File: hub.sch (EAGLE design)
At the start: 50 parts, among them IC1 SN65220DBV, IC2 SN65220DBV, IC3 SN65220DBV, IC4 SN65220DBV, IC5 SN65220DBV, U1 LM3526-L, X1 12MHz

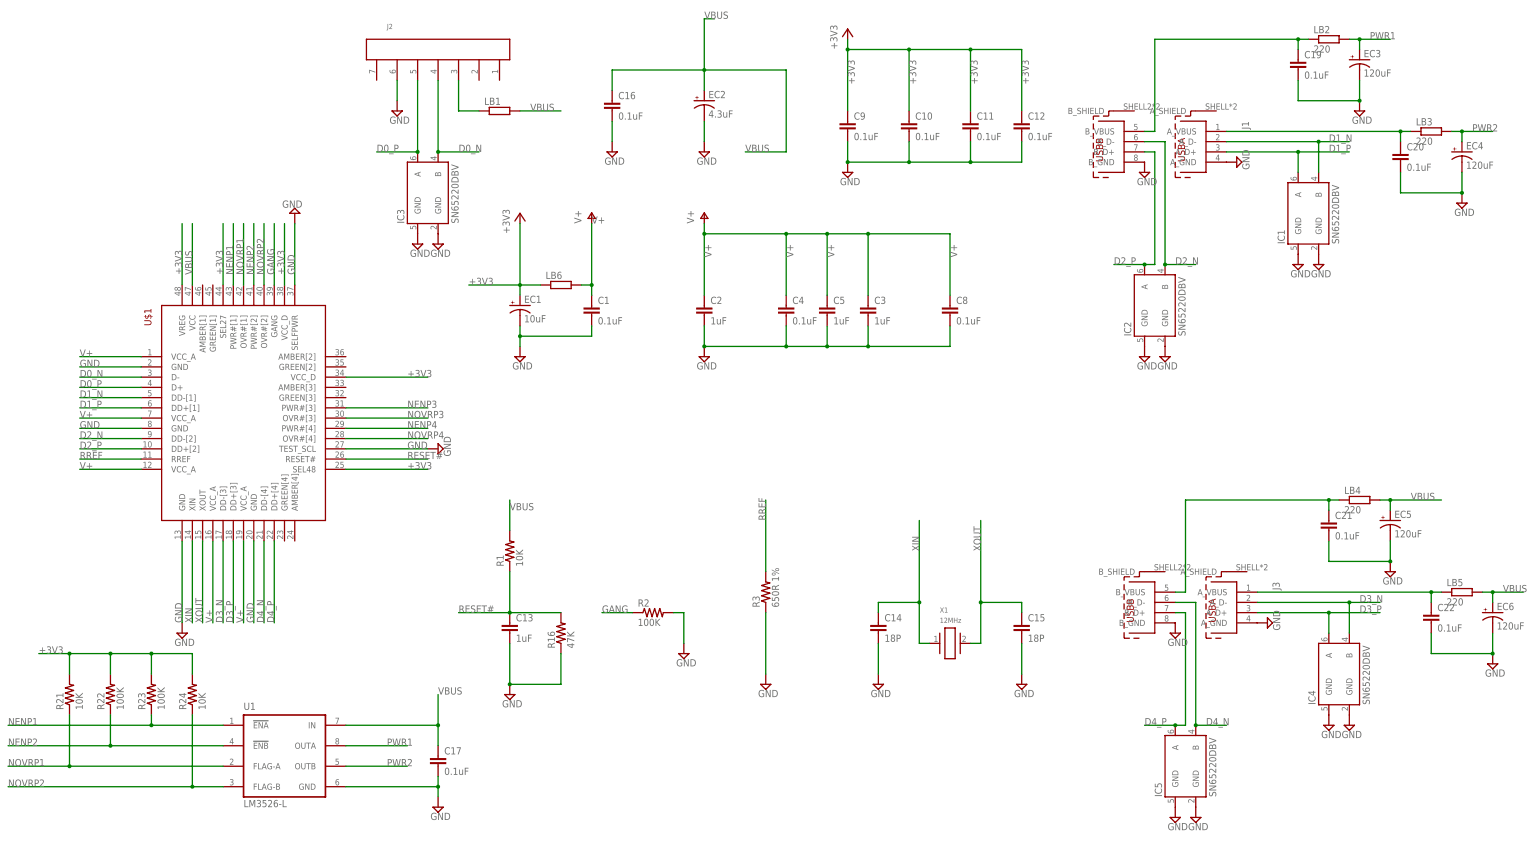
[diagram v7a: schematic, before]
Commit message: pick USB transient suppressors
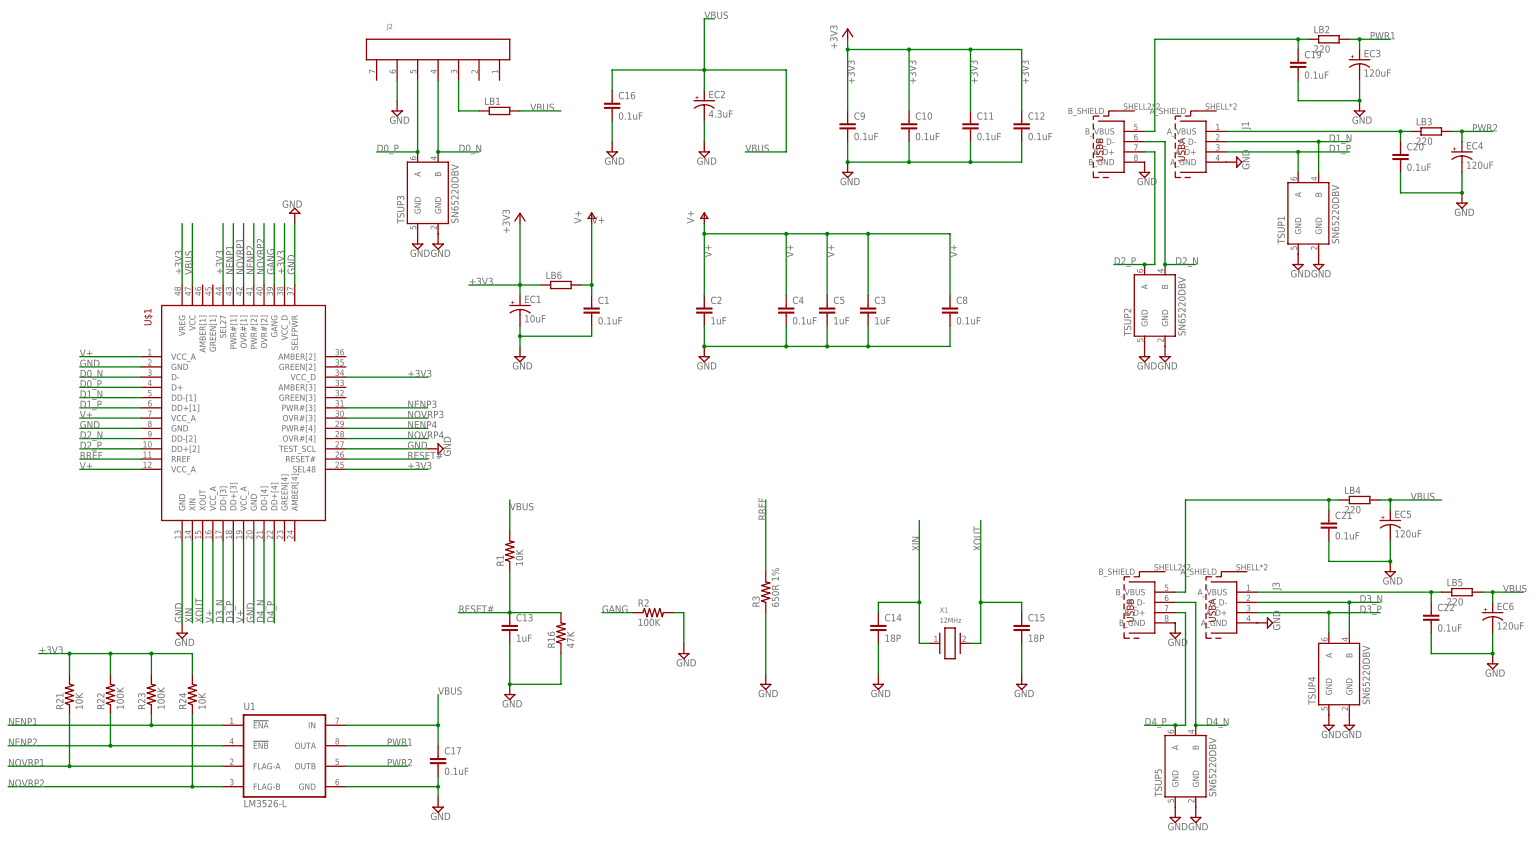
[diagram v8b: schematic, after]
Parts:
- TSUP1, TSUP2, TSUP3, TSUP4, TSUP5: DIGIKEY (none) -> 296-9694-1-ND; MPN (none) -> SN65220DBVR; OC_MOUSER (none) -> 595-SN65220DBVR
- renumbered IC1 to TSUP1, IC2 to TSUP2, IC3 to TSUP3, IC4 to TSUP4, IC5 to TSUP5
